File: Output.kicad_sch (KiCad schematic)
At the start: 18 parts, among them U401 74ACT157, U402 74ACT157, U403 74ACT574

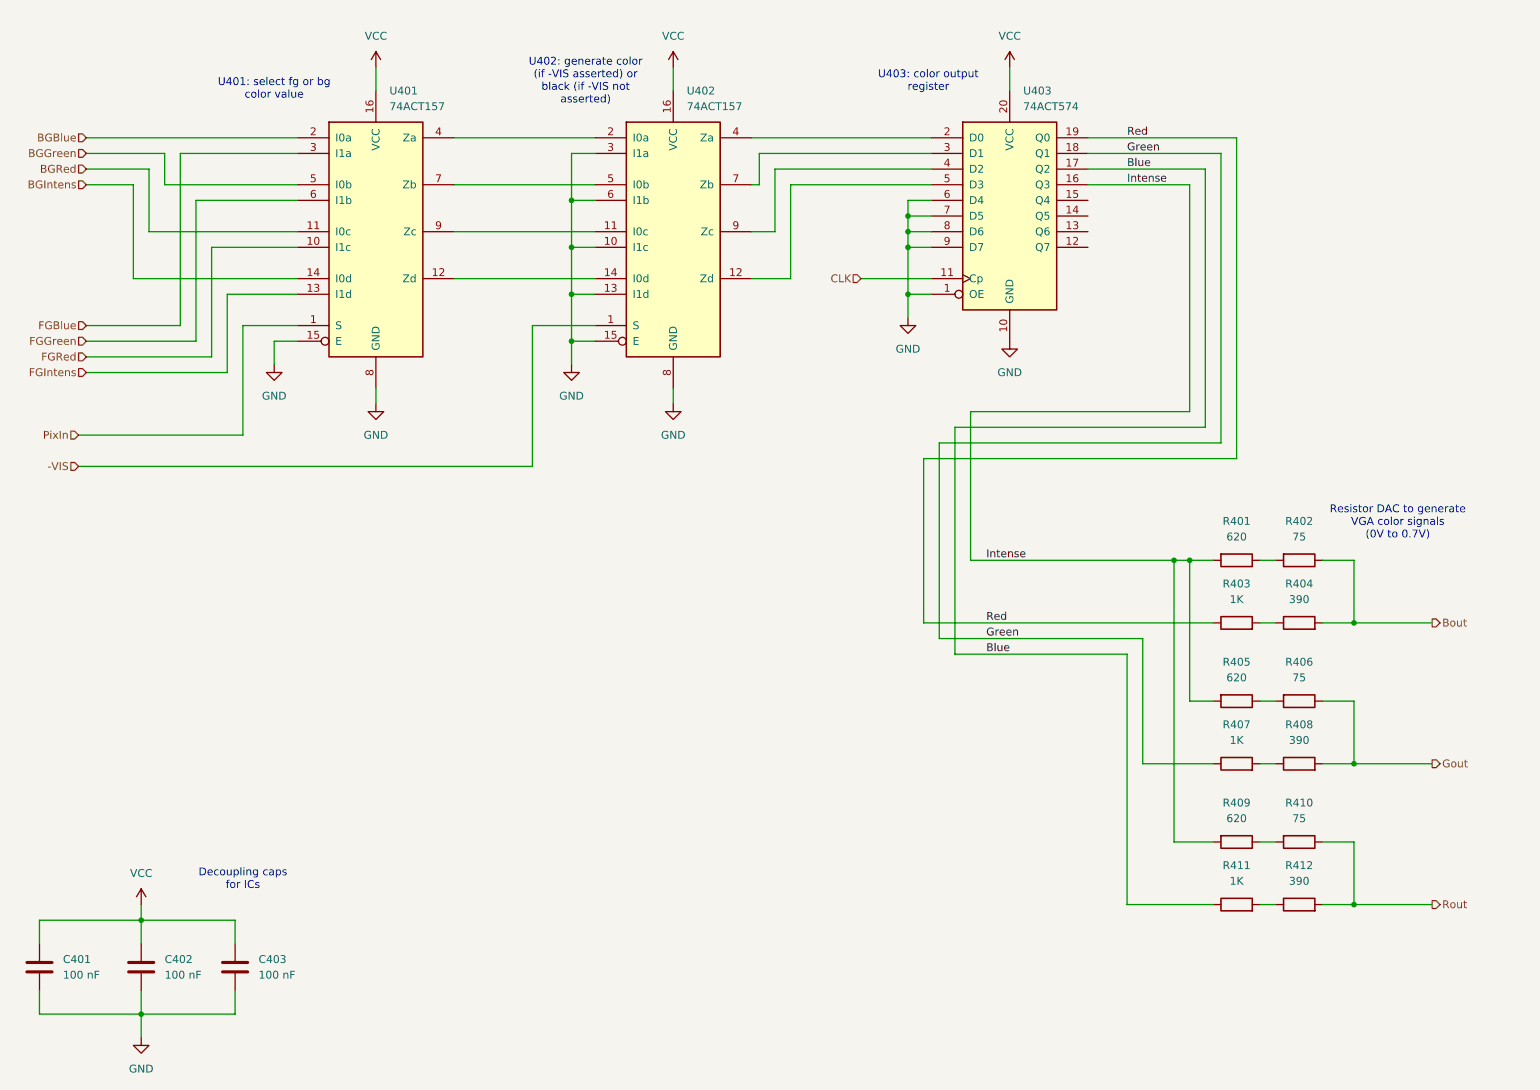
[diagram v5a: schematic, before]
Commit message: use outpt reg for HSync and VSync
This will ensure that they are generated in sync with
the color outputs.

Also, added an output connector for the generated
VGA signals, and fixed the inputs to the resistor DAC.
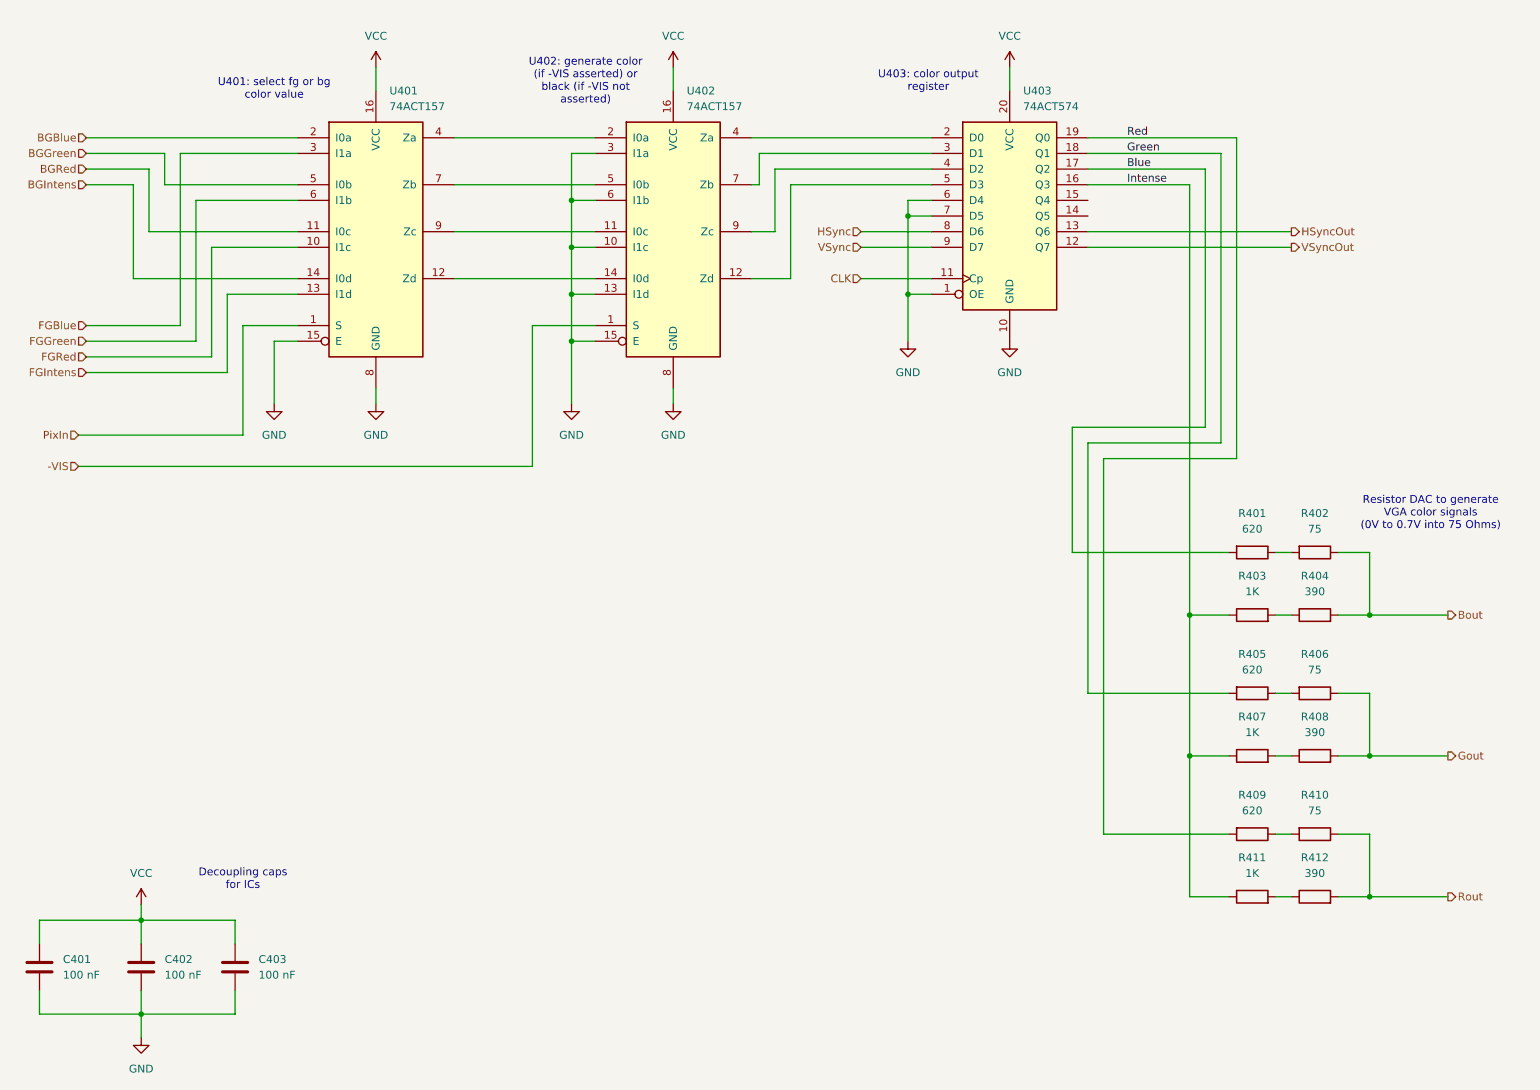
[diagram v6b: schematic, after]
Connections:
- net Blue: now also R401.2; no longer R411.1
- net GND: no longer U403.8 (D6), U403.9 (D7)
- net Green: now also R405.2; no longer R407.1
- net Intense: now also R403.1, R407.1, R411.1; no longer R401.2, R405.2, R409.2
- net Red: now also R409.2; no longer R403.1
- net VSyncOut: now reaches U403.12 (Q7)
- net HSyncOut: now reaches U403.13 (Q6)
- new net HSync: U403.8 (D6)
- new net VSync: U403.9 (D7)
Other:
- note added: "Resistor DAC to generate VGA color signals (0V to 0.7V into 75 Ohms)"
- note removed: "Resistor DAC to generate VGA color signals (0V to 0.7V)"
- moved on the sheet: R401, R402, R403, R404, R405, R406, R407, R408, R409, R410, R411, R412

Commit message: minor fix to Output module
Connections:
- net BGBlue: now also U401.11 (I0c); no longer U401.2 (I0a)
- net BGRed: now also U401.2 (I0a); no longer U401.11 (I0c)
- net FGBlue: now also U401.10 (I1c); no longer U401.3 (I1a)
- net FGRed: now also U401.3 (I1a); no longer U401.10 (I1c)
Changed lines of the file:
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@@
 	(hierarchical_label "FGRed"
 		(shape input)
-		(at 34.29 73.66 180)
+		(at 34.29 68.58 180)
 		(fields_autoplaced yes)
 		(effects
@@
 	(hierarchical_label "BGRed"
 		(shape input)
-		(at 34.29 43.18 180)
+		(at 34.29 38.1 180)
 		(fields_autoplaced yes)
 		(effects
@@
 	(hierarchical_label "FGBlue"
 		(shape input)
-		(at 34.29 68.58 180)
+		(at 34.29 73.66 180)
 		(fields_autoplaced yes)
 		(effects
@@
 	(hierarchical_label "BGBlue"
 		(shape input)
-		(at 34.29 38.1 180)
+		(at 34.29 43.18 180)
 		(fields_autoplaced yes)
 		(effects
